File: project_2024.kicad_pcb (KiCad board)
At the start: 2 copper layers, 128 x 128 mm, 0 parts

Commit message: autogenerated files
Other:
- outline, holes or cut-outs redrawn
- net class default removed

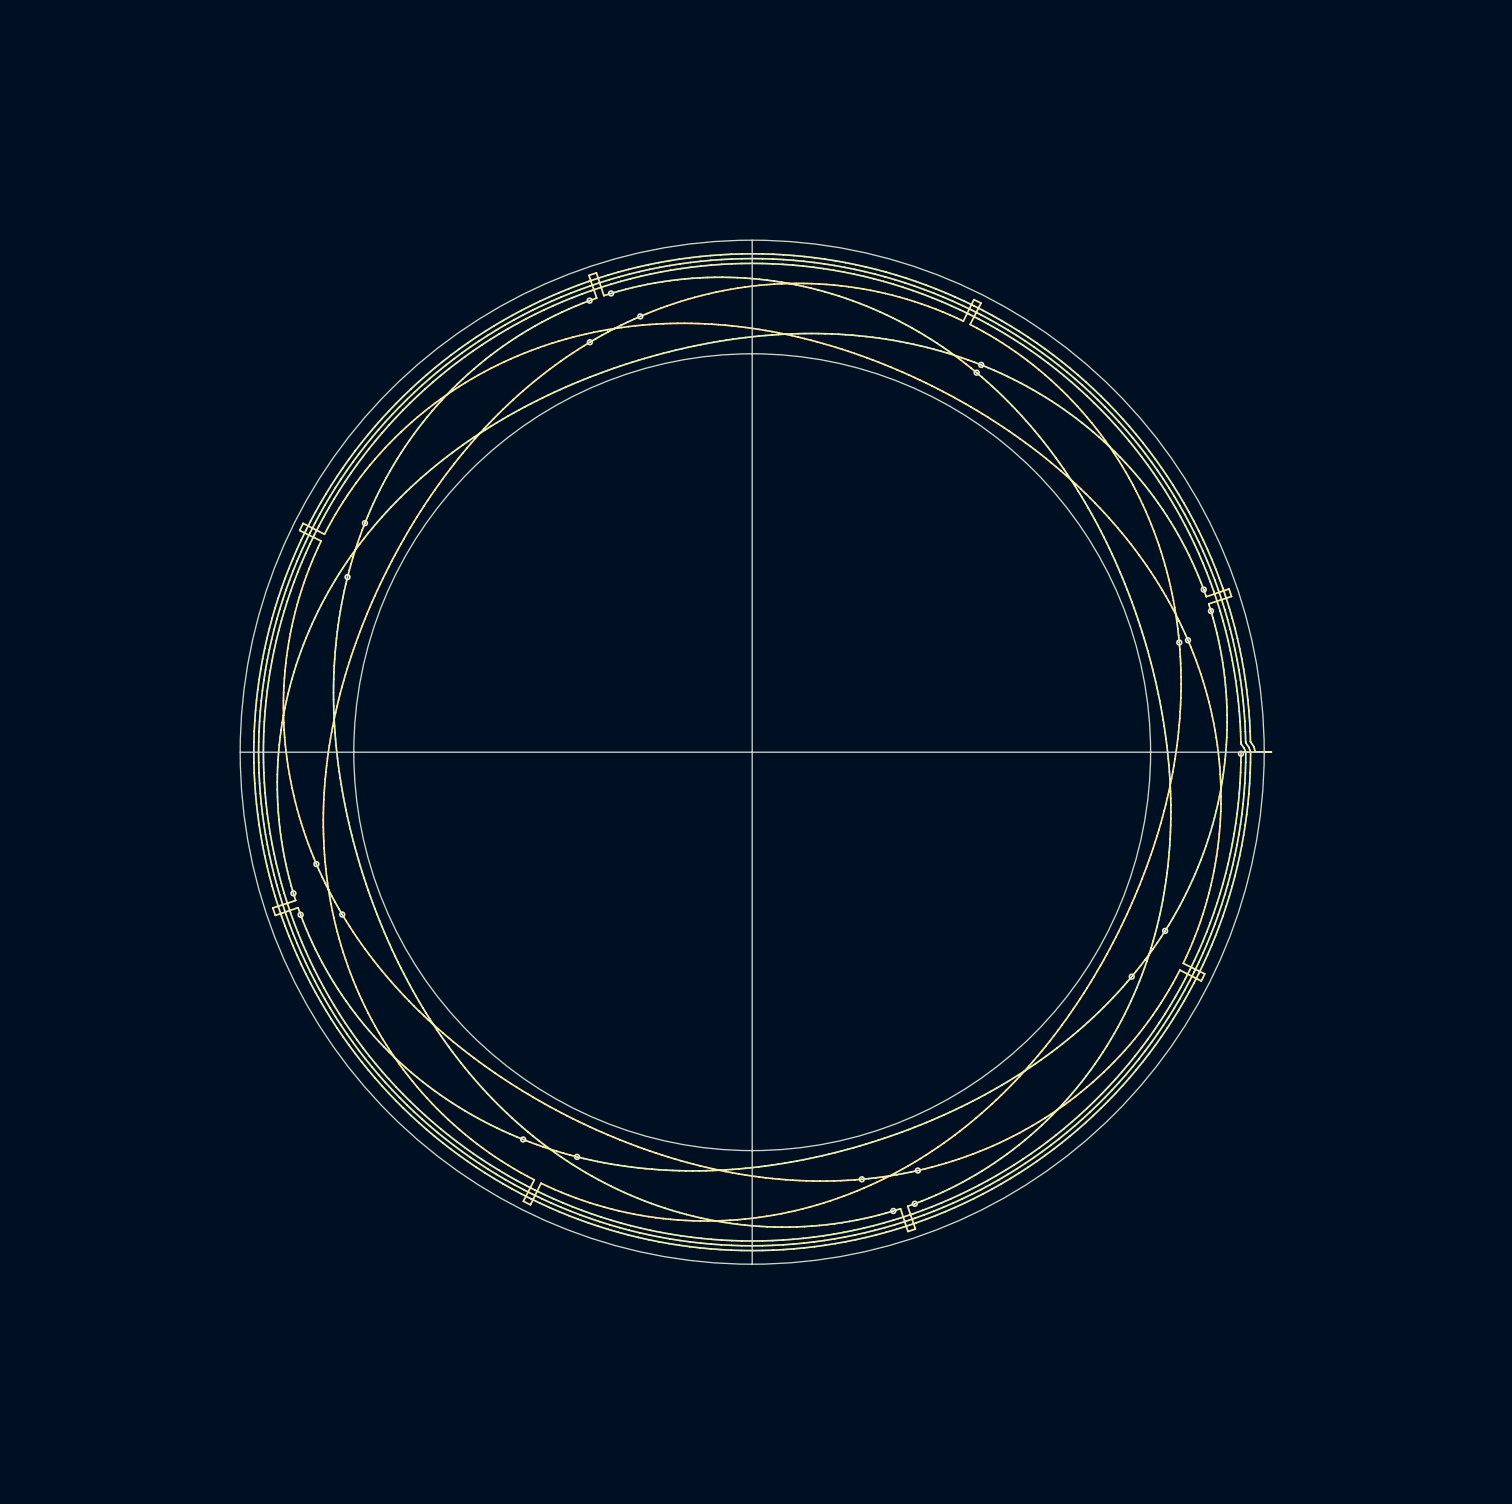
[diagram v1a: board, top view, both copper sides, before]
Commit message: starting layout for 118-220mm induction encoder
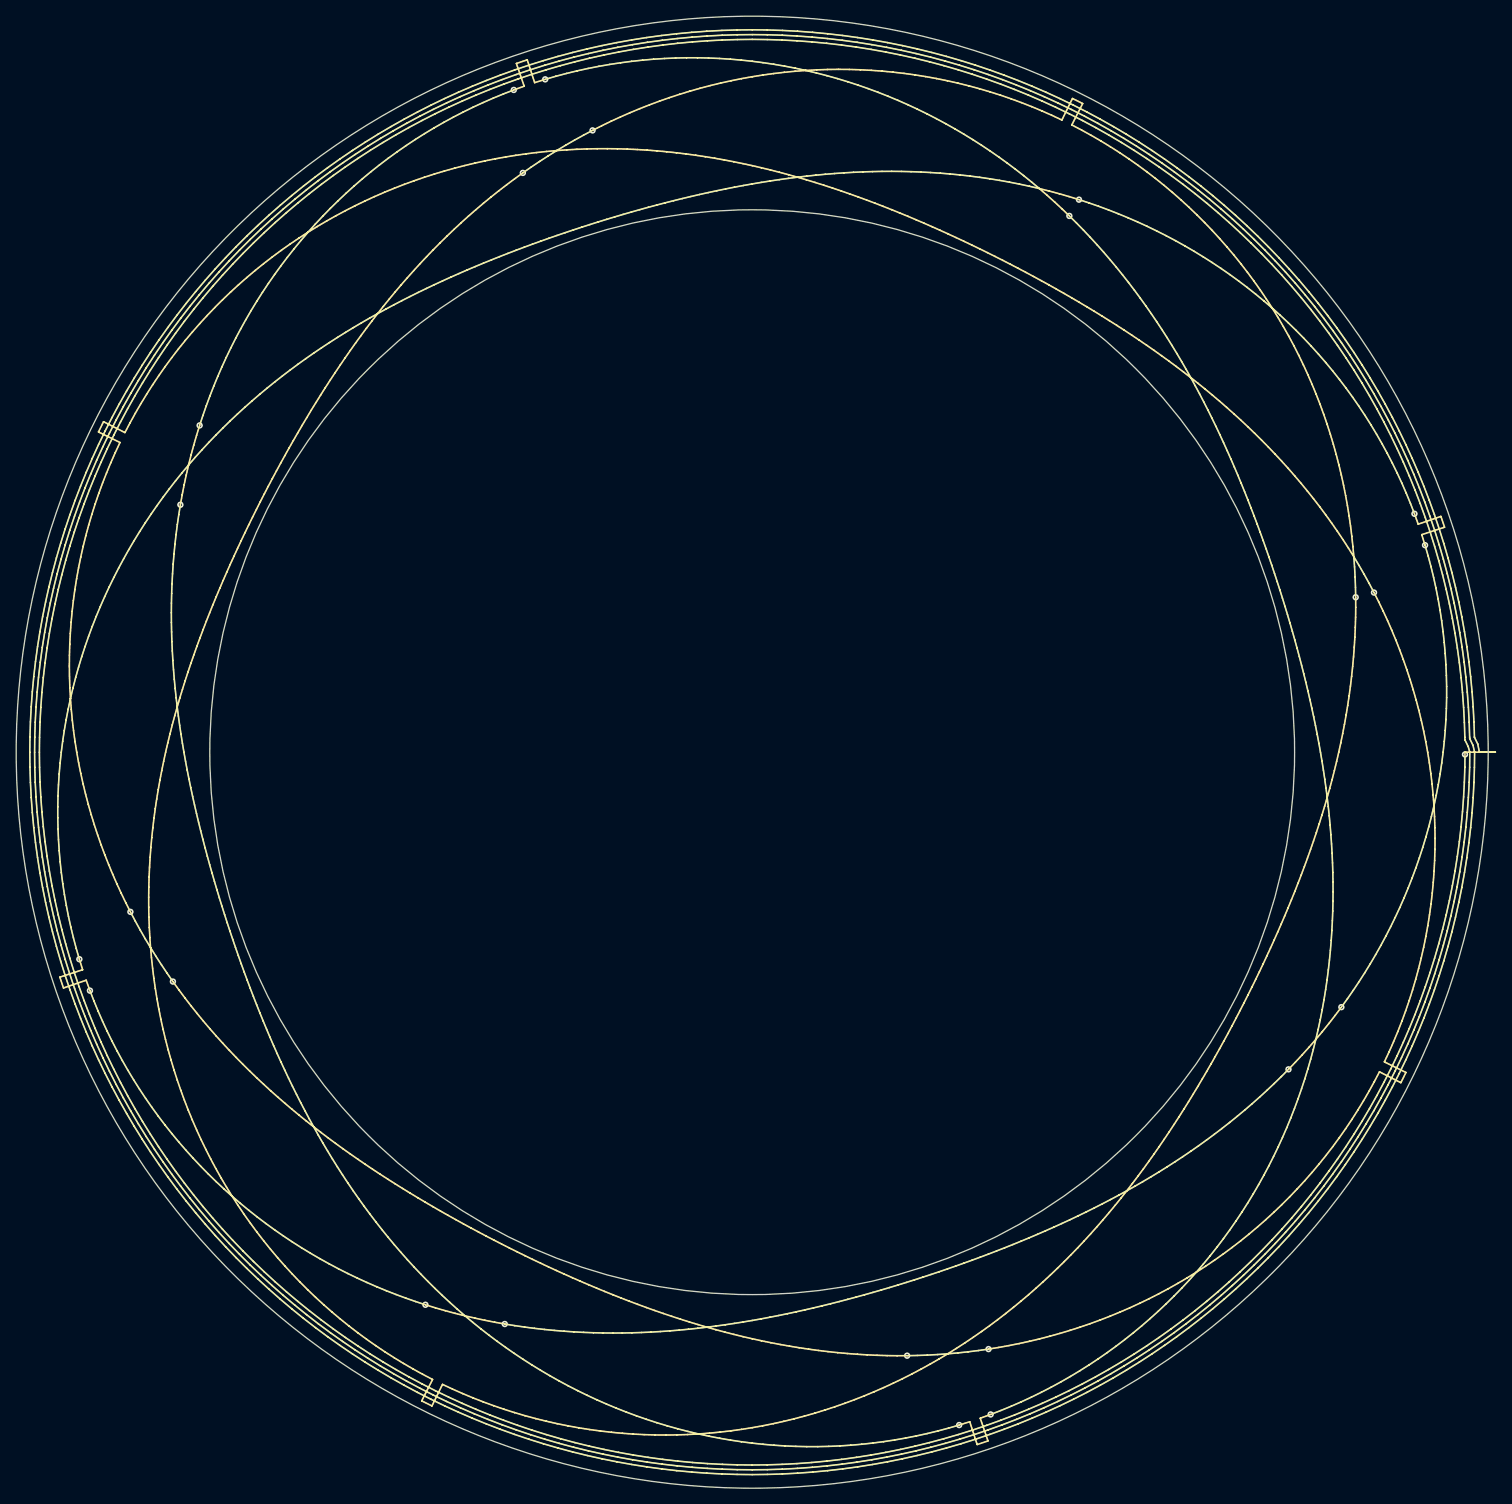
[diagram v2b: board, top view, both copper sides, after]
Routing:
- net TX: track 1169.3 -> 1696.9 mm
- net 2: track 727.3 -> 1028.6 mm
- net 1: track 727.3 -> 1028.6 mm
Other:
- board size 128 x 128 mm -> 184 x 184 mm
- net class default added: trace_width 1
